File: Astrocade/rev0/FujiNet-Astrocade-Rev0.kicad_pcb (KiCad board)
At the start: 6 copper layers, 96 x 58 mm, 100 parts, among them J1 Astrocade_Cart_Edge_26, J2 microSD, J3 USB-C, SW1 BOOTSEL, SW2 S3_RST, SW3 S3_BOOT, SW4 RESET, U1 RP2354A, U2 ESP32-S3-WROOM-1-N16R8, U3 CP2102N-A02-GQFN28, U4 UMH3N, U5 AP63203WU, U6 AP2112K-3.3, Y1 12MHz

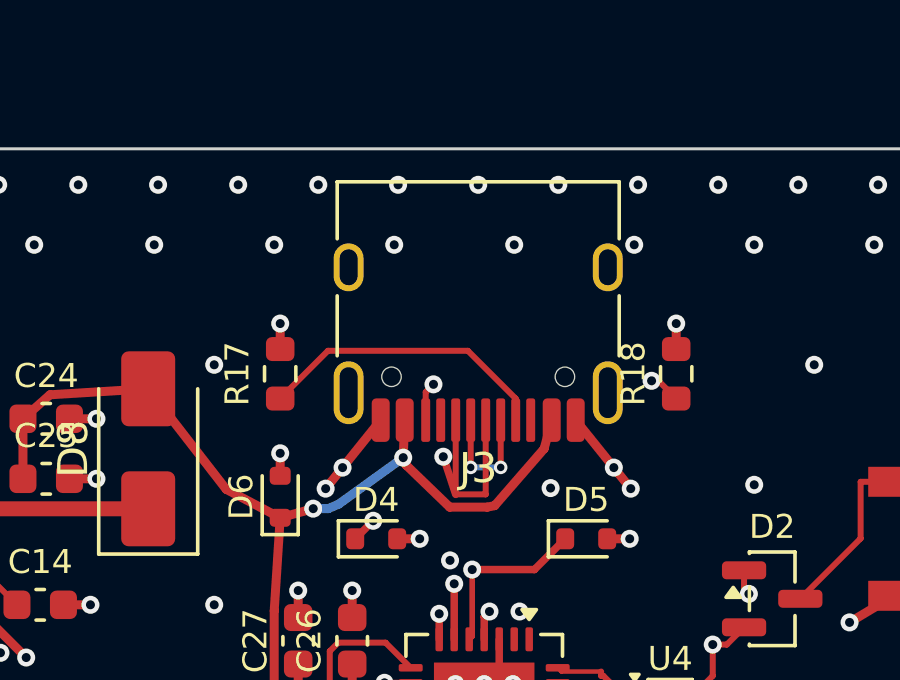
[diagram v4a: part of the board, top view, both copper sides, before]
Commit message: Astrocade Rev0: fix the microSD / USB-C alignment (J3 to the board edge, 3D models)
The same defect as NES Rev0: every cart copies the same HRO USB-C and SOFNG
TF-015 footprints and set_models.py rows.

- J3's shell face sat 1.35 mm inside the trailing edge, where a plug's
  overmold meets the PCB before the plug mates. HRO's recommended layout
  puts the edge at footprint y +3.19 (face 0.46 mm past it): J3 moves
  (124, 35) -> (124, 33.2). tools/usbc_to_edge.py, no re-route: the ties
  and the CC2 via move with J3 (its In2.Cu segment stretches), eight
  1.8 mm F.Cu stubs join the new pad centres to the old ones. The CC1 run
  west would have met R17 pad 2: it now drops at x 118.15, between R17
  and a strip of pour that keeps the rear slot's west F.Cu spoke. Front
  silk past the edge dropped; a Dwgs.User line marks HRO's edge.
- J3's 3D model: offset (0, -1.045, 0), not (0, +1.42, 0).
- J2's 3D model: offset (-0.9, -5.5, 0), not (0, 0, 0); make_tf015_fp.py
  too. J2's copper and position unchanged.

KiCad DRC at every severity with schematic parity on the saved fills:
0 errors, 0 unconnected, 0 parity; no new warning (75, one silk overlap
fewer). check_vias and check_plane_shorts clean. Drill changes: J3's
slots and pegs and the moved CC2 via; the CPL changes J3's Y only.

Co-Authored-By: Claude Opus 5.5 <noreply@anthropic.com>
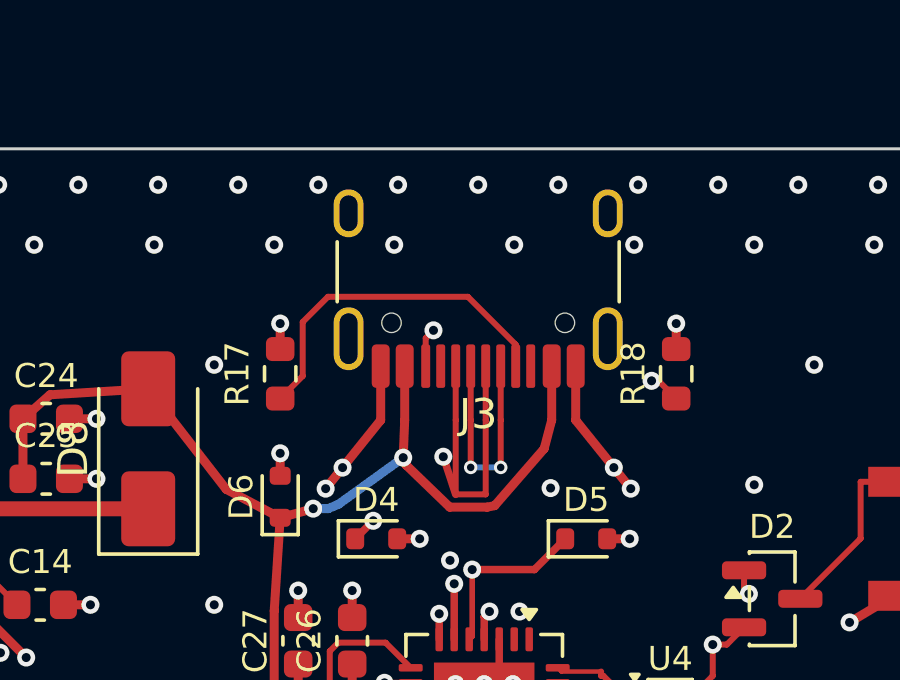
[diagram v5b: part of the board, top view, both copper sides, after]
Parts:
- moved J3 1.80 mm to (124.0, 33.2)
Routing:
- net VBUS: track 33.6 -> 37.2 mm
- net GND: track 88.9 -> 92.5 mm
- net /usb/UBRG_DP: track 20.5 -> 24.1 mm
- net /usb/UBRG_DM: track 13.5 -> 17.1 mm
- net /usb/CC1: track 9.89 -> 11.7 mm
- net /usb/CC2: track 11.4 -> 11.9 mm
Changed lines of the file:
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@@
 	(footprint "FujiNet-Astrocade:USB_C_Receptacle_HRO_TYPE-C-31-M-12"
 		(layer "F.Cu")
-		(at 124 35 180)
-		(descr "USB Type-C receptacle for USB 2.0 and PD, http://www.krhro.com/uploads/soft/180320/1-1P320120243.pdf")
+		(at 124 33.2 180)
+		(descr "USB Type-C receptacle for USB 2.0 and PD, http://www.krhro.com/uploads/soft/180320/1-1P320120243.pdf; PCB edge at y 3.19 (HRO recommended layout: 5.79 mm in front of the pegs), the shell face overhangs it by 0.46 mm")
 		(tags "usb usb-c 2.0 pd")
 		(property "Reference" "J3"
@@
 		(duplicate_pad_numbers_are_jumpers no)
 		(fp_line
-			(start 4.7 2)
-			(end 4.7 3.9)
-			(stroke
-				(width 0.12)
-				(type solid)
-			)
-			(layer "F.SilkS")
-		)
-		(fp_line
 			(start 4.7 -1.9)
 			(end 4.7 0.1)
@@
 		)
 		(fp_line
-			(start -4.7 3.9)
-			(end 4.7 3.9)
-			(stroke
-				(width 0.12)
-				(type solid)
-			)
-			(layer "F.SilkS")
-		)
-		(fp_line
-			(start -4.7 2)
-			(end -4.7 3.9)
+			(start -4.7 -1.9)
+			(end -4.7 0.1)
 			(stroke
 				(width 0.12)
@@
 		)
 		(fp_line
-			(start -4.7 -1.9)
-			(end -4.7 0.1)
+			(start -5.32 3.19)
+			(end 5.32 3.19)
 			(stroke
-				(width 0.12)
-				(type solid)
+				(width 0.1)
+				(type dash)
 			)
-			(layer "F.SilkS")
+			(layer "Dwgs.User")
 		)
 		(fp_line
@@
 		(model "${KIPRJMOD}/3d/USB-C_HRO_TYPE-C-31-M-12.step"
 			(offset
-				(xyz 0 1.42 0)
+				(xyz 0 -1.045 0)
 			)
 			(scale
@@
 		(model "${KIPRJMOD}/3d/TF-015.step"
 			(offset
-				(xyz 0 0 0)
+				(xyz -0.9 -5.5 0)
 			)
 			(scale
@@
 	)
 	(segment
+		(start 127.25 37.245)
+		(end 127.25 39.045)
+		(width 0.3)
+		(layer "F.Cu")
+		(net "GND")
+	)
+	(segment
 		(start 124.7 47.3859)
 		(end 124.7 47.175)
@@
 		(net "GND")
 	)
+	(segment
+		(start 120.75 37.245)
+		(end 120.75 39.045)
+		(width 0.3)
+		(layer "F.Cu")
+		(net "GND")
+	)
 	(via
 		(at 77.2 65.2)
@@
 	)
 	(segment
+		(start 124.25 37.245)
+		(end 124.25 39.045)
+		(width 0.2)
+		(layer "F.Cu")
+		(net "/usb/UBRG_DP")
+	)
+	(segment
 		(start 123.25 41.52)
 		(end 122.836 40.2642)
@@
 	)
 	(segment
+		(start 123.25 37.245)
+		(end 123.25 39.045)
+		(width 0.2)
+		(layer "F.Cu")
+		(net "/usb/UBRG_DP")
+	)
+	(segment
 		(start 123.25 41.52)
 		(end 123.25 39.045)
@@
 	)
 	(segment
+		(start 124.75 37.245)
+		(end 124.75 39.045)
+		(width 0.2)
+		(layer "F.Cu")
+		(net "/usb/UBRG_DM")
+	)
+	(segment
+		(start 123.75 37.245)
+		(end 123.75 39.045)
+		(width 0.2)
+		(layer "F.Cu")
+		(net "/usb/UBRG_DM")
+	)
+	(segment
 		(start 126.9 43)
 		(end 125.874 44.0261)
@@
 	)
 	(segment
-		(start 122.25 38.1105)
-		(end 122.509 37.8514)
+		(start 122.25 36.3105)
+		(end 122.509 36.0514)
 		(width 0.2)
 		(layer "F.Cu")
@@
 	)
 	(segment
-		(start 122.25 39.045)
-		(end 122.25 38.1105)
+		(start 122.25 37.245)
+		(end 122.25 36.3105)
 		(width 0.2)
 		(layer "F.Cu")
@@
 	)
 	(via
-		(at 122.509 37.8514)
+		(at 122.509 36.0514)
 		(size 0.6)
 		(drill 0.3)
@@
 	(segment
 		(start 125.226 37.8514)
-		(end 122.509 37.8514)
+		(end 122.509 36.0514)
 		(width 0.2)
 		(layer "In2.Cu")
@@
 	)
 	(segment
+		(start 126.45 37.245)
+		(end 126.45 39.045)
+		(width 0.3)
+		(layer "F.Cu")
+		(net "VBUS")
+	)
+	(segment
 		(start 117.4 42.3)
 		(end 118.5 41.995)
@@
 	)
 	(segment
+		(start 121.55 37.245)
+		(end 121.55 39.045)
+		(width 0.3)
+		(layer "F.Cu")
+		(net "VBUS")
+	)
+	(segment
 		(start 121.6 40.545)
 		(end 121.5 40.295)
@@
 	)
 	(segment
-		(start 125.25 38.3263)
-		(end 123.657 36.7334)
+		(start 125.25 36.5263)
+		(end 123.657 34.9334)
 		(width 0.2)
 		(layer "F.Cu")
@@
 	)
 	(segment
-		(start 125.25 39.045)
-		(end 125.25 38.3263)
+		(start 118.992 34.9334)
+		(end 118.15 35.7754)
 		(width 0.2)
 		(layer "F.Cu")
@@
 	)
 	(segment
-		(start 118.992 36.7334)
+		(start 118.15 37.575)
 		(end 117.4 38.325)
 		(width 0.2)
@@
 	)
 	(segment
-		(start 123.657 36.7334)
-		(end 118.992 36.7334)
+		(start 125.25 37.245)
+		(end 125.25 36.5263)
+		(width 0.2)
+		(layer "F.Cu")
+		(net "/usb/CC1")
+	)
+	(segment
+		(start 118.15 35.7754)
+		(end 118.15 37.575)
+		(width 0.2)
+		(layer "F.Cu")
+		(net "/usb/CC1")
+	)
+	(segment
+		(start 123.657 34.9334)
+		(end 118.992 34.9334)
 		(width 0.2)
 		(layer "F.Cu")
